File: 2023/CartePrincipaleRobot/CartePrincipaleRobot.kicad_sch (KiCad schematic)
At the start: 3 parts

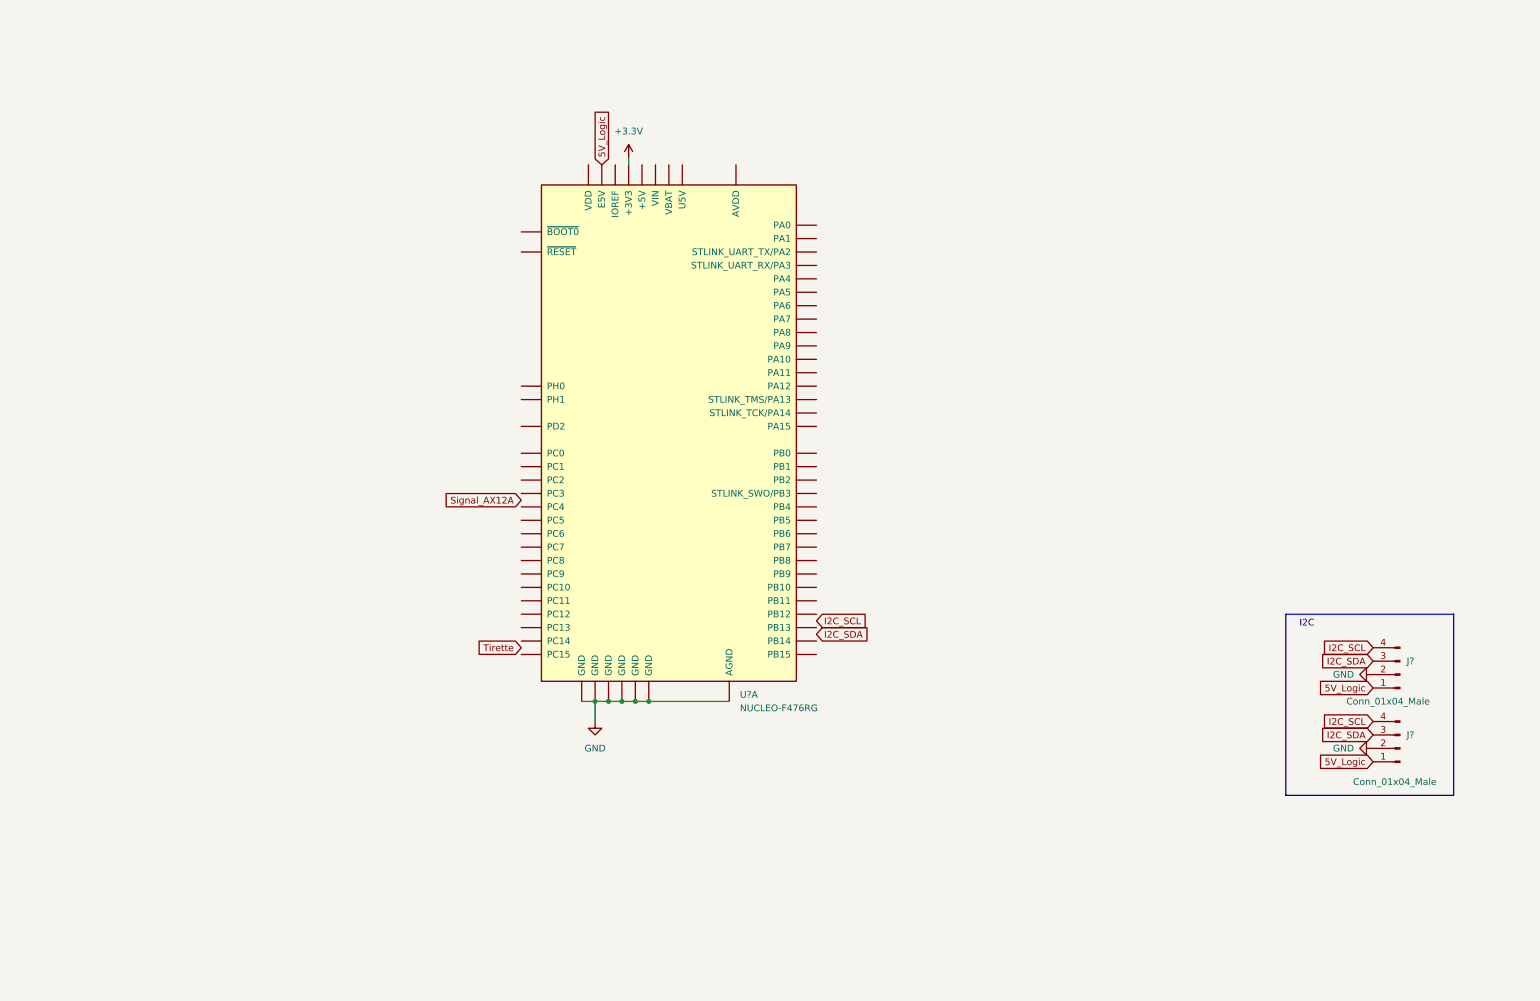
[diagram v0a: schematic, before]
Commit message: Ajout de labels sur le schématique, tome1
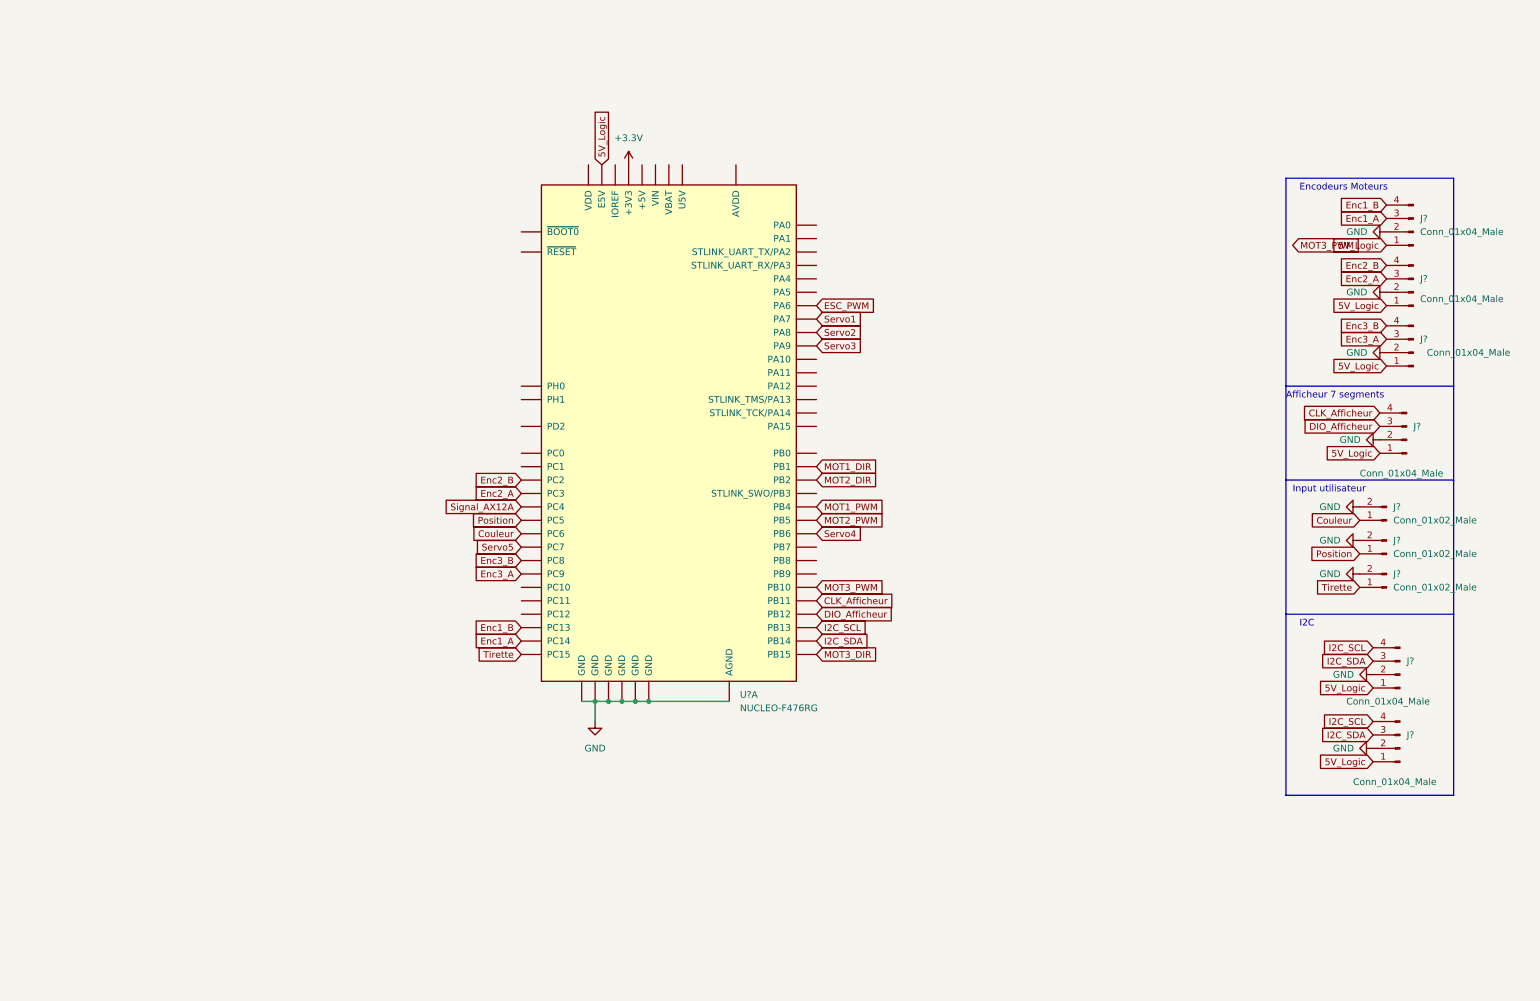
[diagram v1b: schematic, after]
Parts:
- added J? (x3): Conn_01x02_Male, symbol Connector:Conn_01x02_Male
- added J? (x4): Conn_01x04_Male, symbol Connector:Conn_01x04_Male
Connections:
- net 5V_Logic: now also J?.1 (Pin_1), J?.1 (Pin_1), J?.1 (Pin_1), J?.1 (Pin_1)
- net GND: now also J?.2 (Pin_2), J?.2 (Pin_2), J?.2 (Pin_2), J?.2 (Pin_2), J?.2 (Pin_2), J?.2 (Pin_2), J?.2 (Pin_2)
- net I2C_SCL: now also U?.68 (PB13)
- net I2C_SDA: now also U?.66 (PB14)
- net Signal_AX12A: now also U?.72 (PC4)
- net Tirette: now also U?.27 (PC15), J?.1 (Pin_1)
- net Enc1_B: now reaches U?.23 (PC13)
- net Enc1_B: now also J?.4 (Pin_4)
- net Enc1_A: now reaches U?.25 (PC14)
- net Enc1_A: now also J?.3 (Pin_3)
- net Enc2_B: now reaches U?.35 (PC2)
- net Enc2_B: now also J?.4 (Pin_4)
- net Enc2_A: now reaches U?.37 (PC3)
- net Enc2_A: now also J?.3 (Pin_3)
- net Enc3_A: now reaches U?.39 (PC9)
- net Enc3_A: now also J?.3 (Pin_3)
- net Enc3_B: now reaches U?.40 (PC8)
- net Enc3_B: now also J?.4 (Pin_4)
- net Couleur: now reaches U?.42 (PC6)
- net Couleur: now also J?.1 (Pin_1)
- net Position: now reaches U?.44 (PC5)
- net Position: now also J?.1 (Pin_1)
- net ESC_PWM: now reaches U?.51 (PA6)
- net Servo1: now reaches U?.53 (PA7)
- net DIO_Afficheur: now reaches U?.54 (PB12)
- net DIO_Afficheur: now also J?.3 (Pin_3)
- net Servo4: now reaches U?.55 (PB6)
- net CLK_Afficheur: now reaches U?.56 (PB11)
- net CLK_Afficheur: now also J?.4 (Pin_4)
- net Servo5: now reaches U?.57 (PC7)
- net Servo3: now reaches U?.59 (PA9)
- net MOT2_DIR: now reaches U?.60 (PB2)
- net Servo2: now reaches U?.61 (PA8)
- net MOT1_DIR: now reaches U?.62 (PB1)
- net MOT3_PWM: now reaches U?.63 (PB10)
- net MOT3_DIR: now reaches U?.64 (PB15)
- net MOT1_PWM: now reaches U?.65 (PB4)
- net MOT2_PWM: now reaches U?.67 (PB5)
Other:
- note added: "Afficheur 7 segments"
- note added: "Encodeurs Moteurs"
- note added: "Input utilisateur"

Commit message: Ajout des drivers de steppers + connecté tous les tags
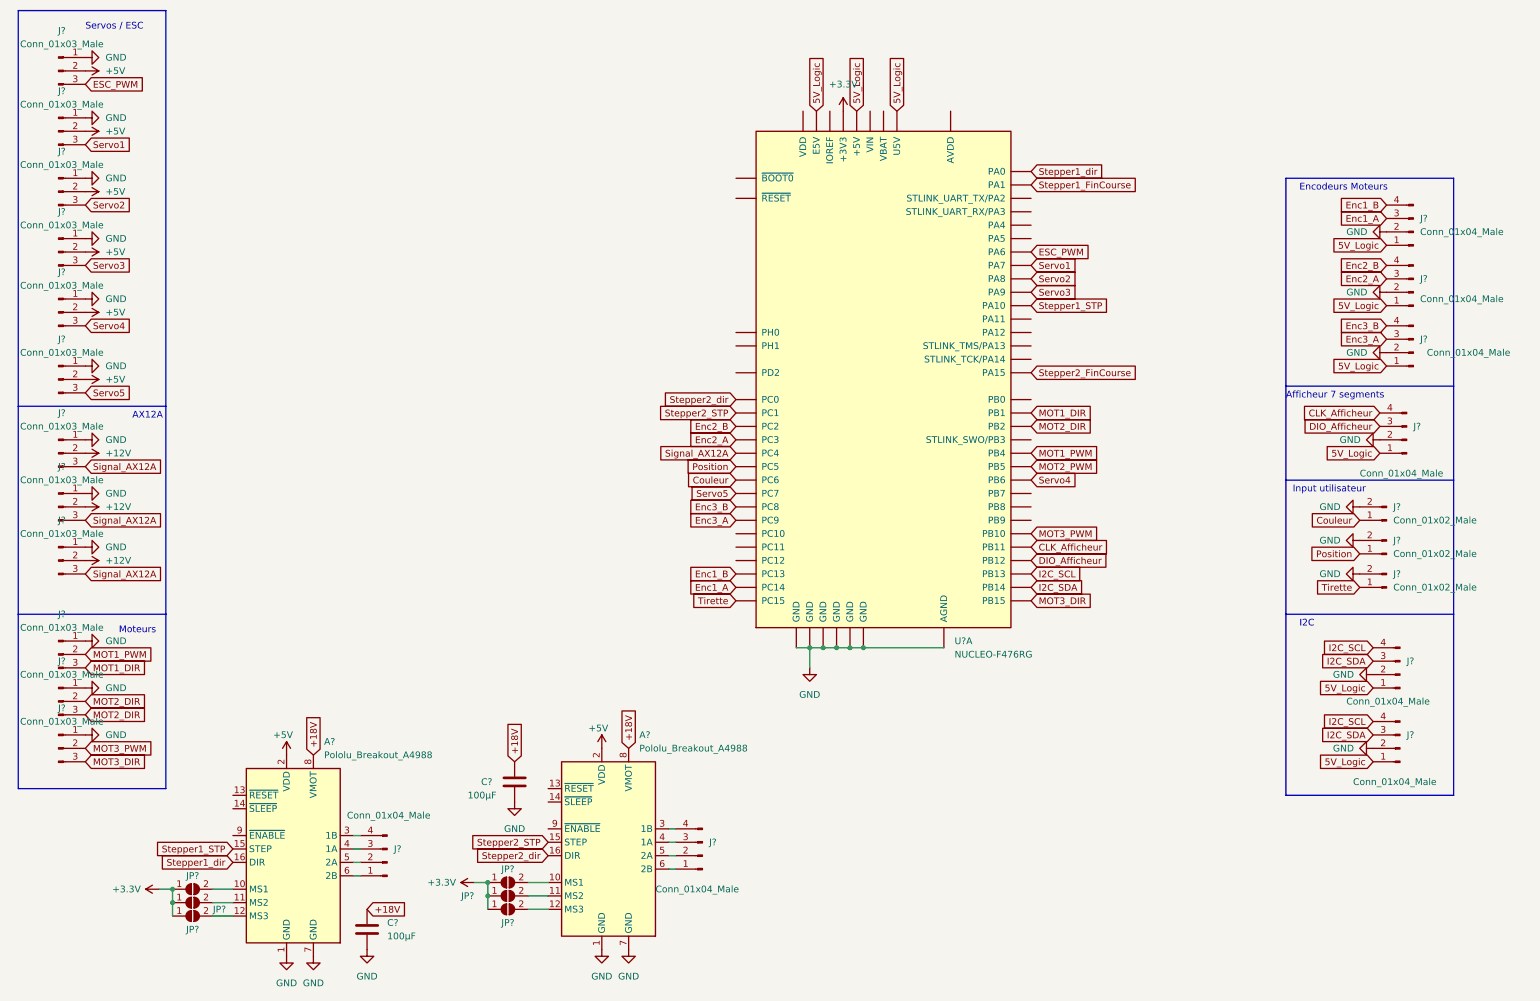
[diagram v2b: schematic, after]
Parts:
- added A? (x2): Pololu_Breakout_A4988, Module:Pololu_Breakout-16_15.2x20.3mm, symbol Driver_Motor:Pololu_Breakout_A4988
- added C? (x2): 100µF, symbol Device:C
- added J? (x12): Conn_01x03_Male, symbol Connector:Conn_01x03_Male
- added J? (x2): Conn_01x04_Male, symbol Connector:Conn_01x04_Male
- added JP? (x6): SolderJumper_2_Open, symbol Jumper:SolderJumper_2_Open
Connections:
- net +3.3V: now also JP?.1 (A), JP?.1 (A), JP?.1 (A), JP?.1 (A), JP?.1 (A), JP?.1 (A)
- net 5V_Logic: now also U?.18 (+5V), U?.46 (U5V)
- net ESC_PWM: now also J?.3 (Pin_3)
- net GND: now also A?.1 (GND), A?.1 (GND), A?.7 (GND), A?.7 (GND), C?.2, C?.2, J?.1 (Pin_1), J?.1 (Pin_1), J?.1 (Pin_1), J?.1 (Pin_1), J?.1 (Pin_1), J?.1 (Pin_1), J?.1 (Pin_1), J?.1 (Pin_1), J?.1 (Pin_1), J?.1 (Pin_1), J?.1 (Pin_1), J?.1 (Pin_1)
- net MOT1_DIR: now also J?.3 (Pin_3)
- net MOT1_PWM: now also J?.2 (Pin_2)
- net MOT2_DIR: now also J?.2 (Pin_2), J?.3 (Pin_3)
- net MOT3_DIR: now also J?.3 (Pin_3)
- net MOT3_PWM: now also J?.2 (Pin_2)
- net Servo1: now also J?.3 (Pin_3)
- net Servo2: now also J?.3 (Pin_3)
- net Servo3: now also J?.3 (Pin_3)
- net Servo4: now also J?.3 (Pin_3)
- net Servo5: now also J?.3 (Pin_3)
- net Signal_AX12A: now also J?.3 (Pin_3), J?.3 (Pin_3), J?.3 (Pin_3)
- net Stepper2_FinCourse: now reaches U?.17 (PA15)
- net Stepper1_dir: now reaches U?.28 (PA0)
- net Stepper1_dir: now also A?.16 (DIR)
- net Stepper1_FinCourse: now reaches U?.30 (PA1)
- net Stepper2_STP: now reaches U?.36 (PC1)
- net Stepper2_STP: now also A?.15 (STEP)
- net Stepper2_dir: now reaches U?.38 (PC0)
- net Stepper2_dir: now also A?.16 (DIR)
- net Stepper1_STP: now reaches U?.71 (PA10)
- net Stepper1_STP: now also A?.15 (STEP)
- new net: A?.10 (MS1), JP?.2 (B) (x2)
- new net: A?.11 (MS2), JP?.2 (B) (x2)
- new net: A?.12 (MS3), JP?.2 (B) (x2)
- new net: A?.3 (1B), J?.4 (Pin_4) (x2)
- new net: A?.4 (1A), J?.3 (Pin_3) (x2)
- new net: A?.5 (2A), J?.2 (Pin_2) (x2)
- new net: A?.6 (2B), J?.1 (Pin_1) (x2)
- new net +12V: J?.2 (Pin_2), J?.2 (Pin_2), J?.2 (Pin_2)
- new net +18V: A?.8 (VMOT), A?.8 (VMOT), C?.1, C?.1
- new net +5V: A?.2 (VDD), A?.2 (VDD), J?.2 (Pin_2), J?.2 (Pin_2), J?.2 (Pin_2), J?.2 (Pin_2), J?.2 (Pin_2), J?.2 (Pin_2)
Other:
- note added: "AX12A"
- note added: "Moteurs"
- note added: "Servos / ESC"
- moved on the sheet: U?A

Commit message: Schéma carte principale fini
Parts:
- added J1, J2: Conn_01x02_Male, symbol Connector:Conn_01x02_Male
- added J15, J16, J17: Screw_Terminal_01x02, symbol Connector:Screw_Terminal_01x02
- added U1: TSR_1-2450, Converter_DCDC:Converter_DCDC_TRACO_TSR-1_THT, symbol Regulator_Switching:TSR_1-2450
- gave numbers to parts that had none: 34
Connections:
- net +12V: now also J17.1 (Pin_1)
- net +18V: now also J16.1 (Pin_1), U1.1 (Vin)
- net +3.3V: now also A1.13 (~{RESET}), A1.14 (~{SLEEP}), A2.13 (~{RESET}), A2.14 (~{SLEEP})
- net +5V: now also U1.3 (Vout)
- net 5V_Logic: now also J15.1 (Pin_1)
- net GND: now also A1.9 (~{ENABLE}), A2.9 (~{ENABLE}), J1.1 (Pin_1), J15.2 (Pin_2), J16.2 (Pin_2), J17.2 (Pin_2), J2.1 (Pin_1), U1.2 (GND)
- net MOT2_DIR: no longer J13.2 (Pin_2)
- net MOT2_PWM: now also J13.2 (Pin_2)
- net Stepper1_FinCourse: now also J2.2 (Pin_2)
- net Stepper2_FinCourse: now also J1.2 (Pin_2)
- no-connect marks 0 -> 26
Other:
- note added: "Alim"
- note added: "Fin course steppers"
- note added: "Steppers"
- moved on the sheet: A1, A2, C1, C2, J18, J19, JP1, JP2, JP3, JP4, JP5, JP6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

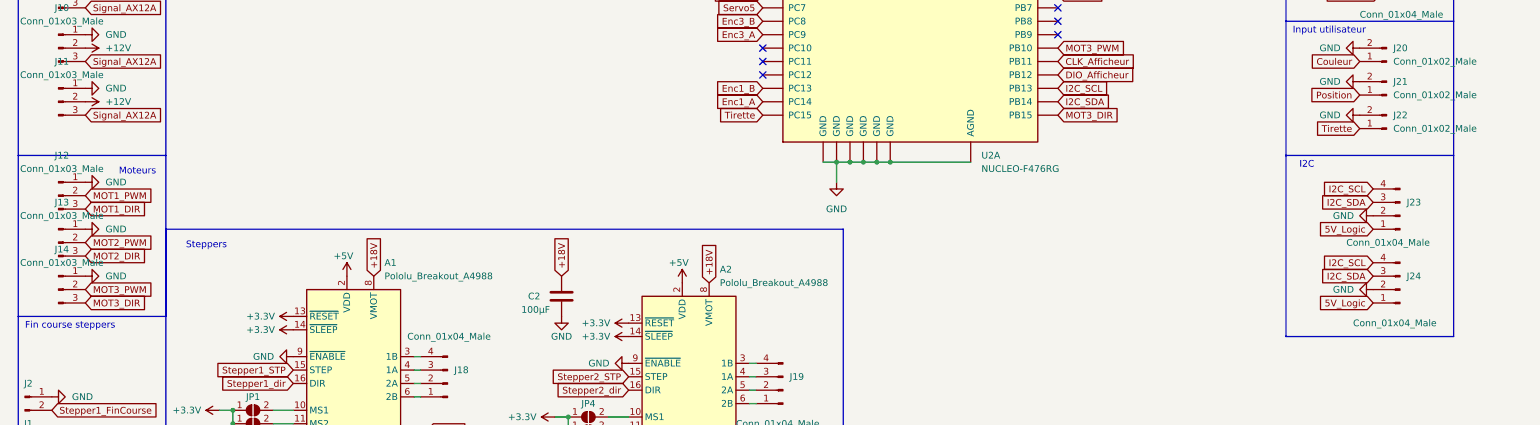
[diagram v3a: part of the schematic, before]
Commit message: Ajout de résistances de pullup
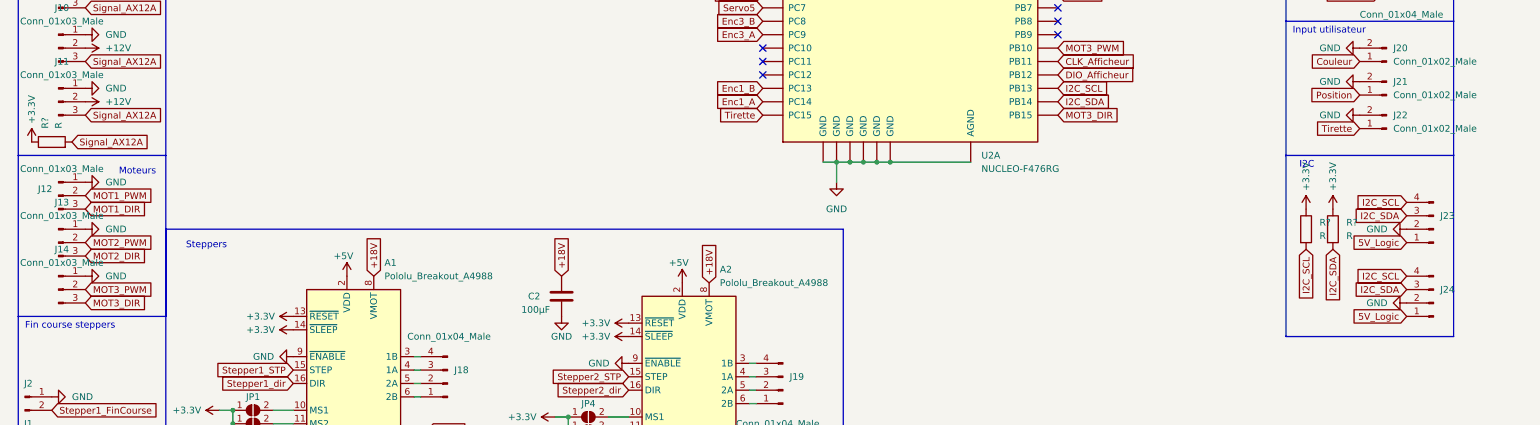
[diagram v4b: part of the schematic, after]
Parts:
- added R? (x3): R, symbol Device:R
- J1, J2, J20, J21, J22: footprint (none) -> library:HE14_EMBASE_1x02
- J10, J11, J12, J13, J14, J3, J4, J5, J6, J7, J8, J9: footprint (none) -> library:HE14_EMBASE_1x03
- J18, J19, J23, J24, J25, J26, J27, J28: footprint (none) -> library:HE14_EMBASE_1x04
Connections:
- net +3.3V: now also R?.1, R?.1, R?.1
- net I2C_SCL: now also R?.2
- net I2C_SDA: now also R?.2
- net Signal_AX12A: now also R?.2
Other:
- moved on the sheet: J23, J24

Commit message: update
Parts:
- C1, C2: footprint (none) -> Capacitor_THT:CP_Radial_D10.0mm_P5.00mm
- J10, J11, J9: footprint library:HE14_EMBASE_1x03 -> Connector_Molex:Molex_SPOX_5267-03A_1x03_P2.50mm_Vertical
- J15, J16, J17: footprint (none) -> TerminalBlock:TerminalBlock_bornier-2_P5.08mm
- J3, J4, J5, J6, J7, J8: footprint library:HE14_EMBASE_1x03 -> Connector_PinSocket_2.54mm:PinSocket_1x03_P2.54mm_Vertical
- JP1, JP2, JP3, JP4, JP5, JP6: footprint (none) -> Jumper:SolderJumper-2_P1.3mm_Open_RoundedPad1.0x1.5mm
- R1: renamed from R?; value R -> 1k; footprint (none) -> Resistor_SMD:R_0805_2012Metric_Pad1.20x1.40mm_HandSolder
- R2, R3: renamed from R?; value R -> 2.2k; footprint (none) -> Resistor_SMD:R_0805_2012Metric_Pad1.20x1.40mm_HandSolder
- U2: footprint ST_NUCLEO-F476RG -> library:ST_NUCLEO-F401RE

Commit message: update
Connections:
- net 5V_Logic: no longer U2.18 (+5V), U2.46 (U5V), U2.6 (E5V)
- no-connect marks 26 -> 28
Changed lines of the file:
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@@
   (no_connect (at 171.45 26.67))
   (no_connect (at 209.55 104.14))
+  (no_connect (at 168.91 26.67))
   (no_connect (at 153.67 109.22))
   (no_connect (at 194.31 26.67))
   (no_connect (at 209.55 81.28))
+  (no_connect (at 184.15 26.67))
   (no_connect (at 153.67 43.18))
   (no_connect (at 209.55 101.6))
@@
     )
   )
-  (global_label "5V_Logic" (shape input) (at 184.15 26.67 90) (fields_autoplaced)
-    (effects (font (size 1.27 1.27)) (justify left))
-    (property "Références Inter-Feuilles" "${INTERSHEET_REFS}" (id 0) (at 184.0706 15.9717 90)
-      (effects (font (size 1.27 1.27)) (justify left) hide)
-    )
-  )
   (global_label "MOT2_DIR" (shape input) (at 25.4 146.05 0) (fields_autoplaced)
     (effects (font (size 1.27 1.27)) (justify left))
@@
     )
   )
-  (global_label "5V_Logic" (shape input) (at 176.53 26.67 90) (fields_autoplaced)
-    (effects (font (size 1.27 1.27)) (justify left))
-    (property "Références Inter-Feuilles" "${INTERSHEET_REFS}" (id 0) (at 176.4506 15.9717 90)
+  (global_label "5V_Logic" (shape input) (at 123.19 26.67 90) (fields_autoplaced)
+    (effects (font (size 1.27 1.27)) (justify left))
+    (property "Références Inter-Feuilles" "${INTERSHEET_REFS}" (id 0) (at 123.1106 15.9717 90)
       (effects (font (size 1.27 1.27)) (justify left) hide)
     )
@@
       (effects (font (size 1.27 1.27)) (justify left) hide)
     )
-  )
-  (global_label "5V_Logic" (shape input) (at 168.91 26.67 90) (fields_autoplaced)
-    (effects (font (size 1.27 1.27)) (justify left))
-    (property "Références Inter-Feuilles" "${INTERSHEET_REFS}" (id 0) (at 168.8306 15.9717 90)
-      (effects (font (size 1.27 1.27)) (justify left) hide)
-    )
